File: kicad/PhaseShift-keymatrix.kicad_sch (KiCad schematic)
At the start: 26 parts

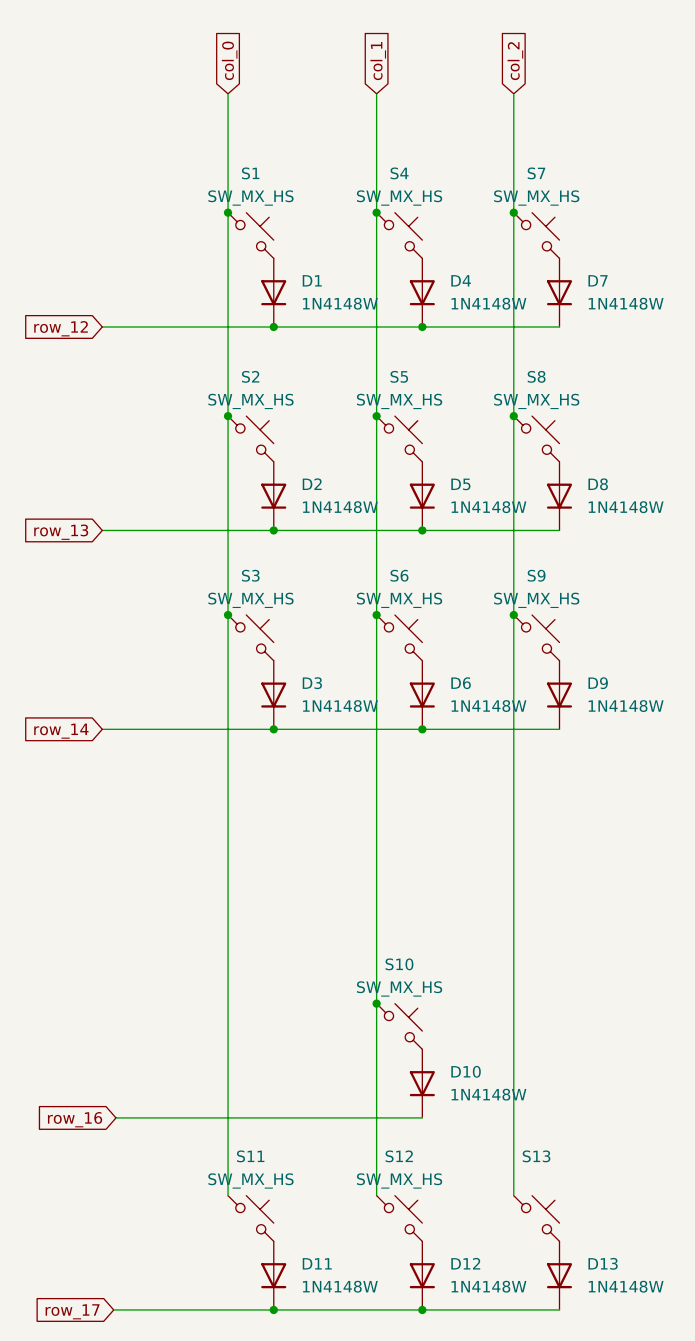
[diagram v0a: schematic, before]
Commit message: added MCU
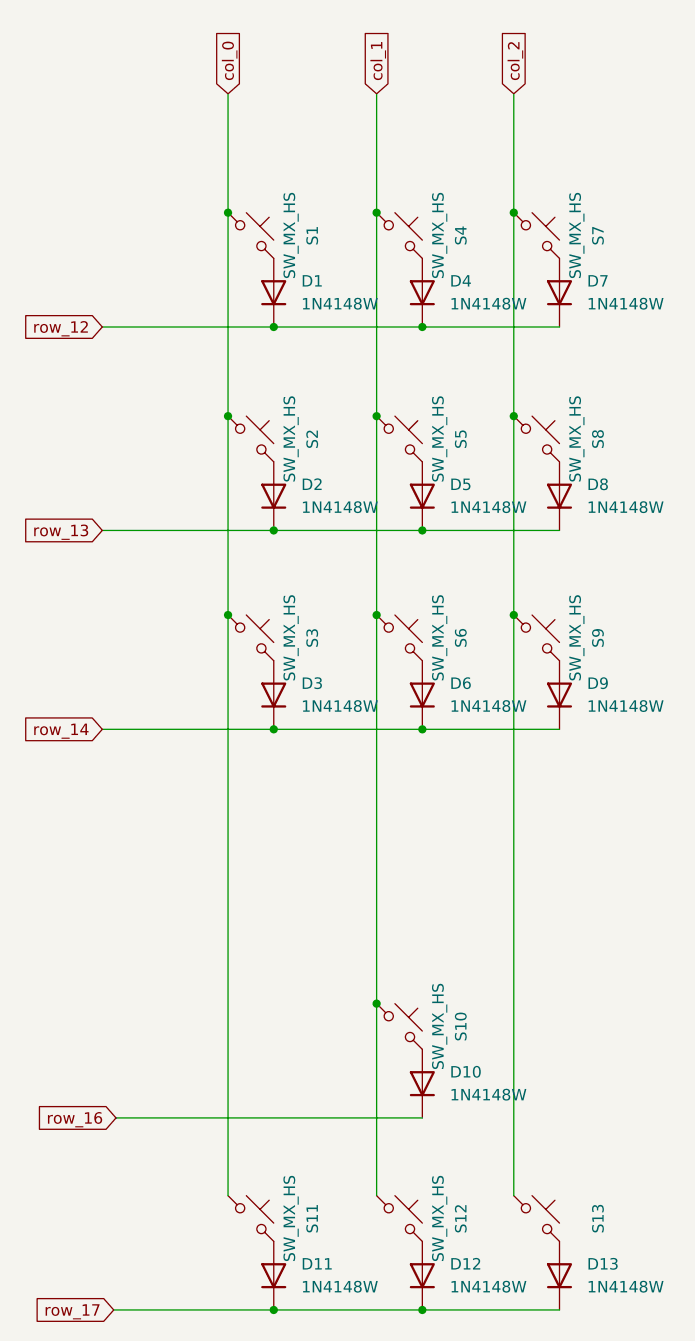
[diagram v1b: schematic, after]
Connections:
- net col_0: now also S1.2, S11.2, S2.2, S3.2; no longer S1.1, S11.1, S2.1, S3.1
- net col_1: now also S10.2, S12.2, S4.2, S5.2, S6.2; no longer S10.1, S12.1, S4.1, S5.1, S6.1
- net col_2: now also S13.2, S7.2, S8.2, S9.2; no longer S13.1, S7.1, S8.1, S9.1
- net at D7.2 (A): now also S7.1; no longer S7.2
- net at D1.2 (A): now also S1.1; no longer S1.2
- net at D9.2 (A): now also S9.1; no longer S9.2
- net at D12.2 (A): now also S12.1; no longer S12.2
- net at D13.2 (A): now also S13.1; no longer S13.2
- net at D6.2 (A): now also S6.1; no longer S6.2
- net at D11.2 (A): now also S11.1; no longer S11.2
- net at D3.2 (A): now also S3.1; no longer S3.2
- net at D5.2 (A): now also S5.1; no longer S5.2
- net at D4.2 (A): now also S4.1; no longer S4.2
- net at D8.2 (A): now also S8.1; no longer S8.2
- net at D2.2 (A): now also S2.1; no longer S2.2
- net at D10.2 (A): now also S10.1; no longer S10.2
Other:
- moved on the sheet: S1, S10, S11, S12, S13, S2, S3, S4, S5, S6, S7, S8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

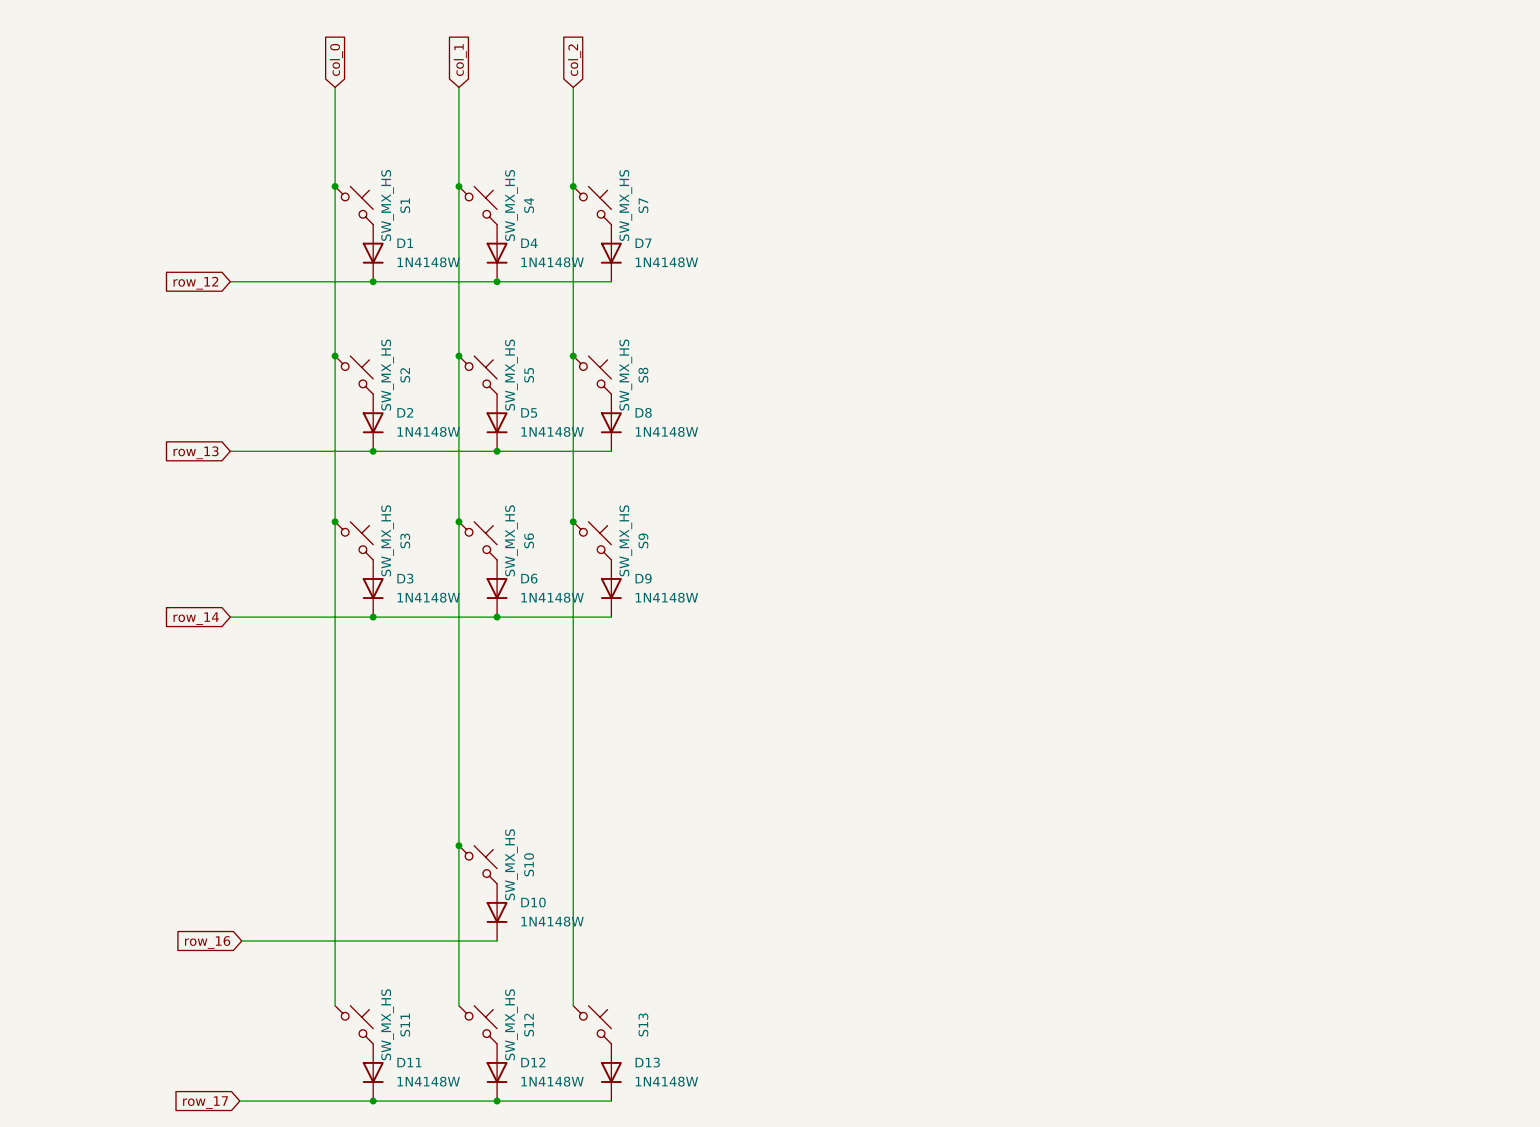
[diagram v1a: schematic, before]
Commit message: pogo pin connectors
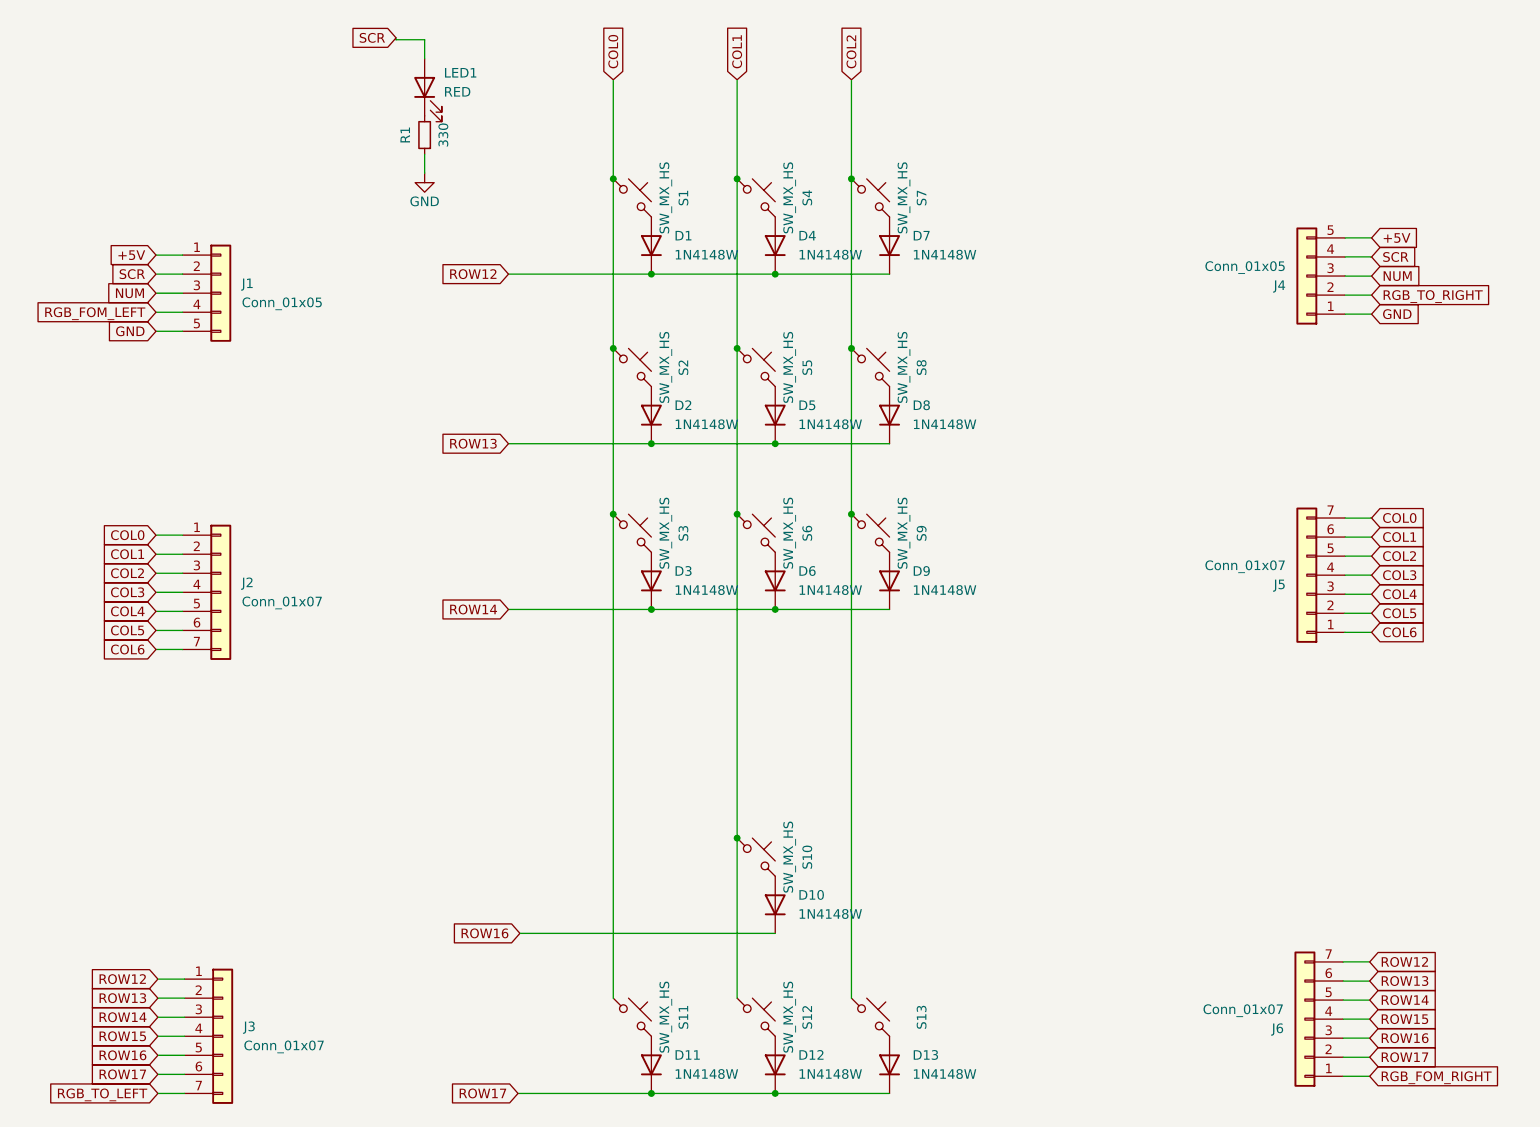
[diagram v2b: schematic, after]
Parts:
- added J1, J4: Conn_01x05, TB2086_MISC:Pogopin_1x05_P2.54mm_Curved, symbol Connector_Generic:Conn_01x05
- added J2, J3, J5, J6: Conn_01x07, symbol Connector_Generic:Conn_01x07
- added LED1: RED, LED_SMD:LED_0603_1608Metric_Pad1.05x0.95mm_HandSolder, symbol Device:LED
- added R1: 330, Resistor_SMD:R_0603_1608Metric, symbol Device:R_Small
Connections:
- net col_0 renamed COL0
- net COL0: now also J2.1 (Pin_1), J5.7 (Pin_7)
- net col_1 renamed COL1
- net COL1: now also J2.2 (Pin_2), J5.6 (Pin_6)
- net col_2 renamed COL2
- net COL2: now also J2.3 (Pin_3), J5.5 (Pin_5)
- net row_12 renamed ROW12
- net ROW12: now also J3.1 (Pin_1), J6.7 (Pin_7)
- net row_13 renamed ROW13
- net ROW13: now also J3.2 (Pin_2), J6.6 (Pin_6)
- net row_14 renamed ROW14
- net ROW14: now also J3.3 (Pin_3), J6.5 (Pin_5)
- net row_16 renamed ROW16
- net ROW16: now also J3.5 (Pin_5), J6.3 (Pin_3)
- net row_17 renamed ROW17
- net ROW17: now also J3.6 (Pin_6), J6.2 (Pin_2)
- new net: LED1.1 (K), R1.2
- new net +5V: J1.1 (Pin_1), J4.5 (Pin_5)
- new net COL3: J2.4 (Pin_4), J5.4 (Pin_4)
- new net COL4: J2.5 (Pin_5), J5.3 (Pin_3)
- new net COL5: J2.6 (Pin_6), J5.2 (Pin_2)
- new net COL6: J2.7 (Pin_7), J5.1 (Pin_1)
- new net GND: J1.5 (Pin_5), J4.1 (Pin_1), R1.1
- new net NUM: J1.3 (Pin_3), J4.3 (Pin_3)
- new net RGB_FOM_LEFT: J1.4 (Pin_4)
- new net RGB_FOM_RIGHT: J6.1 (Pin_1)
- new net RGB_TO_LEFT: J3.7 (Pin_7)
- new net RGB_TO_RIGHT: J4.2 (Pin_2)
- new net ROW15: J3.4 (Pin_4), J6.4 (Pin_4)
- new net SCR: J1.2 (Pin_2), J4.4 (Pin_4), LED1.2 (A)
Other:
- moved on the sheet: D1, D10, D11, D12, D13, D2, D3, D4, D5, D6, D7, D8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

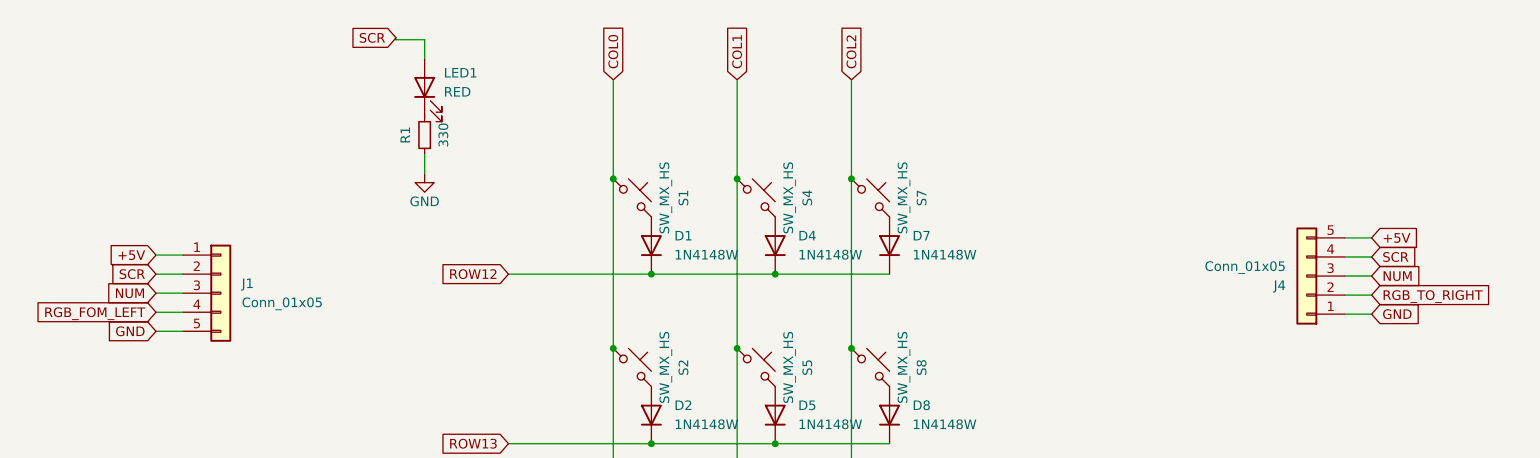
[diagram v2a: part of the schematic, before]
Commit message: screw holes
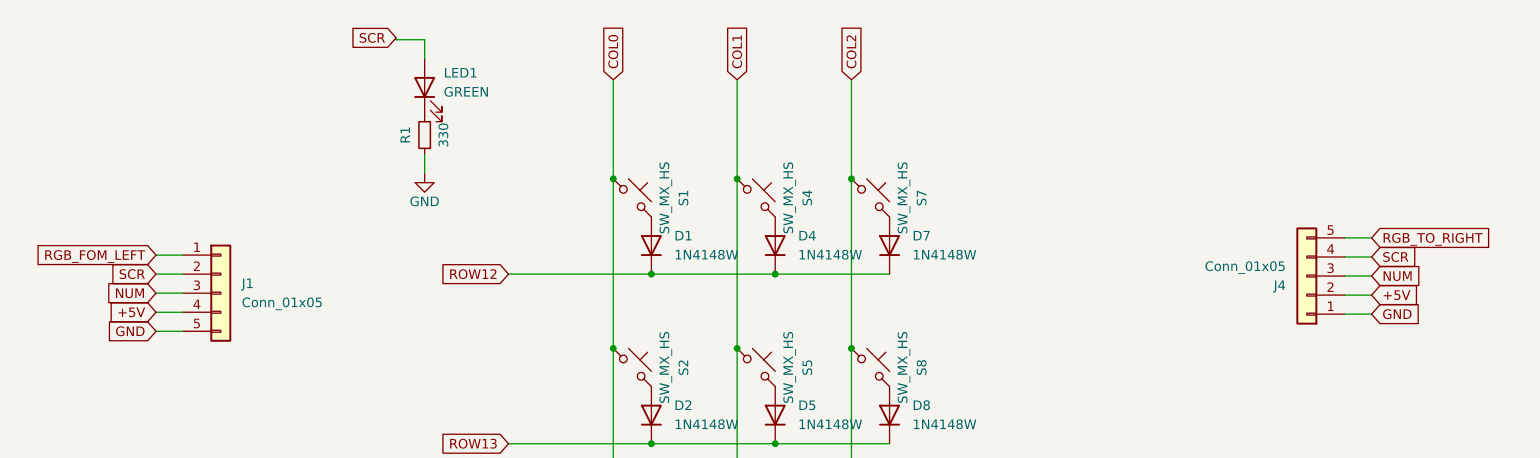
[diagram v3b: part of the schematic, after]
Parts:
- J2, J3, J5, J6: footprint (none) -> TB2086_MISC:Pogopin_1x07_P2.54mm_Curved
- LED1: value RED -> GREEN
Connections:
- net +5V: now also J1.4 (Pin_4), J4.2 (Pin_2); no longer J1.1 (Pin_1), J4.5 (Pin_5)
- net RGB_FOM_LEFT: now also J1.1 (Pin_1); no longer J1.4 (Pin_4)
- net RGB_TO_RIGHT: now also J4.5 (Pin_5); no longer J4.2 (Pin_2)
